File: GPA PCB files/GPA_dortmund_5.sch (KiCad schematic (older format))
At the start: 29 parts, among them U103 AAVID_TO220_HEATSINK, U23 OPA549_KV_11TO-220_11, U24 OPA549_KV_11TO-220_11, U25 INA149SOIC8, X9 MINI-FIT-JR-045569-NA2

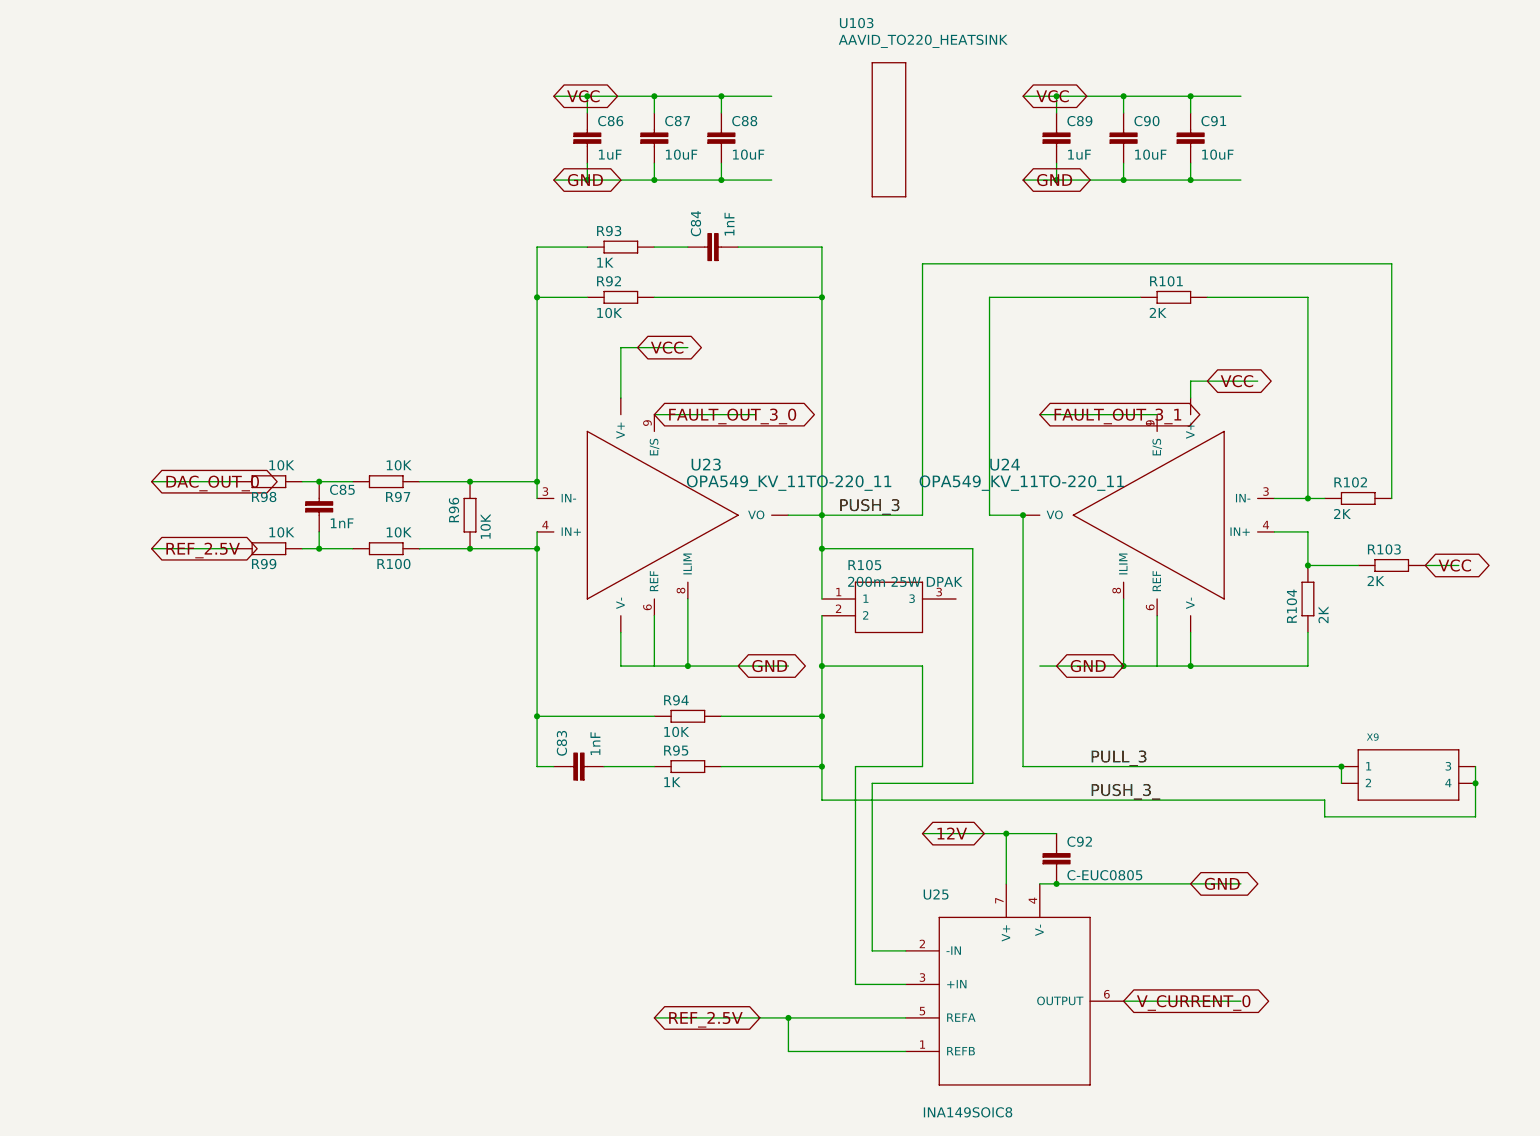
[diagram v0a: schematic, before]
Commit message: fixed schematic after conversion from eagle
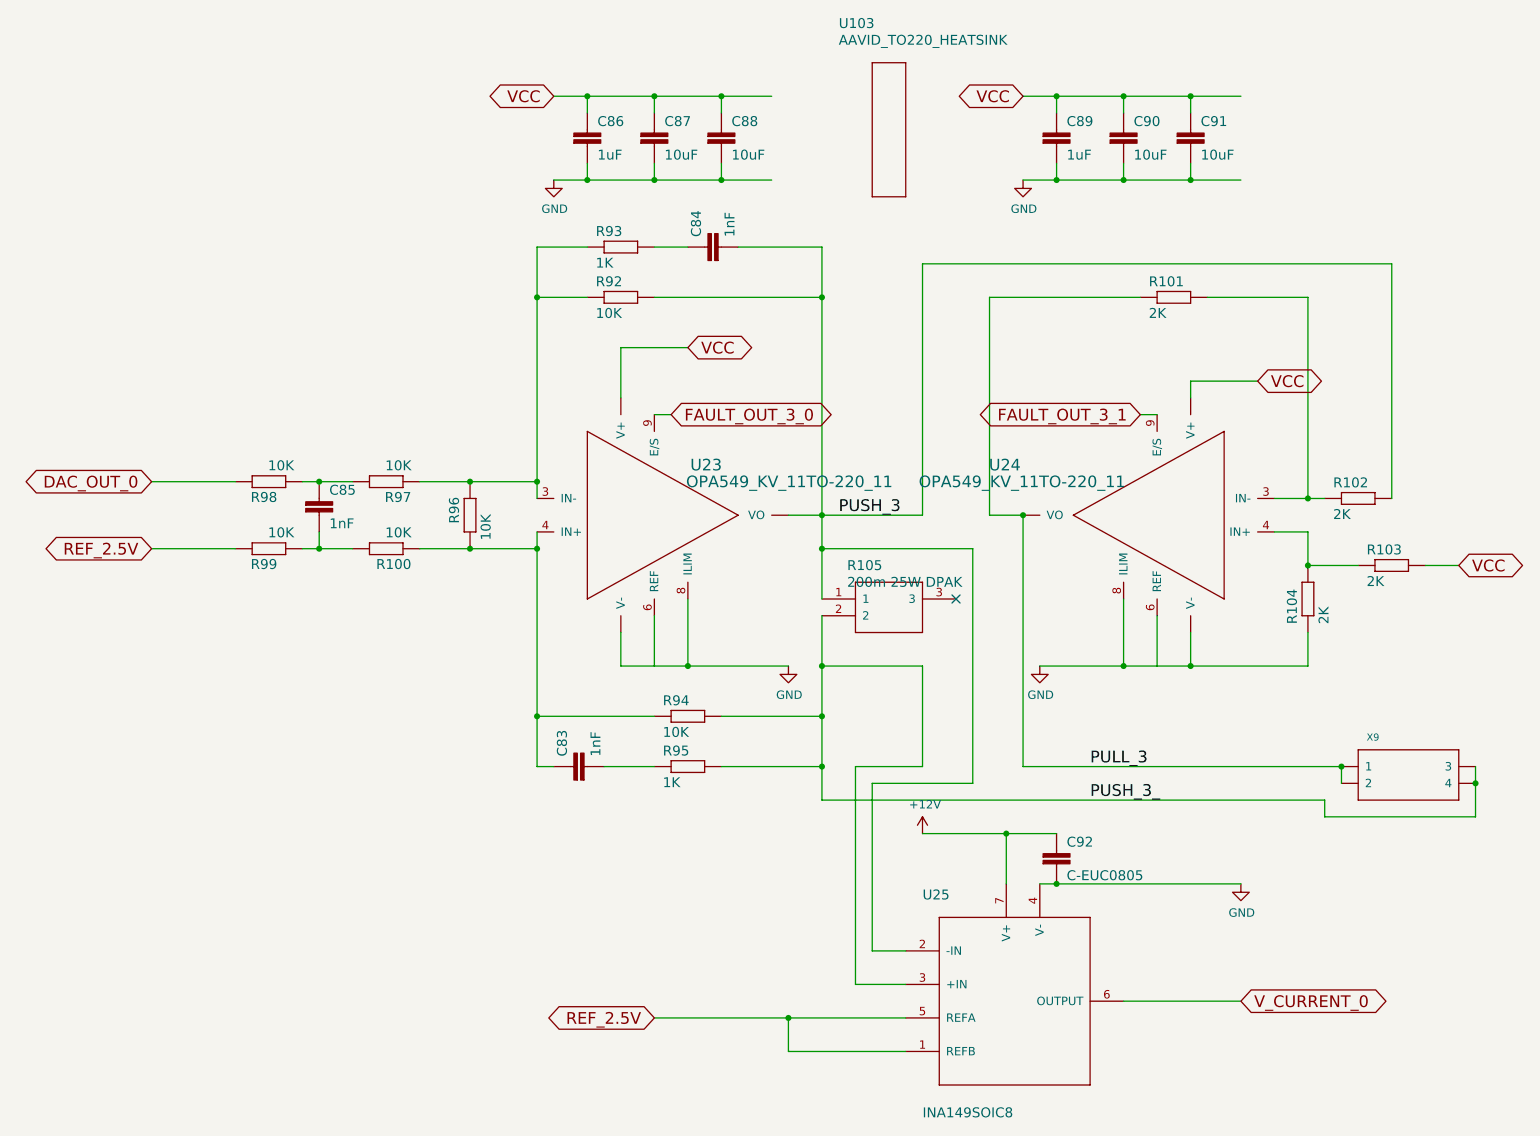
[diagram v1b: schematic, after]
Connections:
- net labels added: +12V
- net labels removed: 12V
- no-connect marks 0 -> 1
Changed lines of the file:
@@
 $Descr A4 11693 8268
 encoding utf-8
-Sheet 1 6
+Sheet 6 6
 Title ""
 Date ""
@@
 Wire Wire Line
 	4600 2800 5000 2800
-Text GLabel 4700 2800 2    70   BiDi ~ 0
+Text GLabel 5000 2800 2    70   BiDi ~ 0
 VCC
 Wire Wire Line
@@
 Wire Wire Line
 	8000 3000 8400 3000
-Text GLabel 8100 3000 2    70   BiDi ~ 0
+Text GLabel 8400 3000 2    70   BiDi ~ 0
 VCC
 Wire Wire Line
 	9400 4100 9600 4100
-Text GLabel 9400 4100 2    70   BiDi ~ 0
+Text GLabel 9600 4100 2    70   BiDi ~ 0
 VCC
 Wire Wire Line
@@
 Connection ~ 4800 1300
 Connection ~ 5200 1300
-Text GLabel 4200 1300 2    70   BiDi ~ 0
+Text GLabel 4200 1300 0    70   BiDi ~ 0
 VCC
 Wire Wire Line
@@
 Connection ~ 7600 1300
 Connection ~ 8000 1300
-Text GLabel 7000 1300 2    70   BiDi ~ 0
+Text GLabel 7000 1300 0    70   BiDi ~ 0
 VCC
 Wire Wire Line
@@
 	5000 4300 5000 4700
 Connection ~ 5000 4700
-Text GLabel 5300 4700 2    70   BiDi ~ 0
-GND
 Wire Wire Line
 	8000 4500 8000 4700
@@
 	8700 4700 8000 4700
 Connection ~ 7600 4700
-Text GLabel 7200 4700 2    70   BiDi ~ 0
-GND
 Connection ~ 8000 4700
 Wire Wire Line
@@
 Connection ~ 4800 1800
 Connection ~ 4400 1800
-Text GLabel 4200 1800 2    70   BiDi ~ 0
-GND
 Wire Wire Line
 	7000 1800 7200 1800
@@
 Connection ~ 7600 1800
 Connection ~ 7200 1800
-Text GLabel 7000 1800 2    70   BiDi ~ 0
-GND
 Wire Wire Line
 	7100 6000 7200 6000
 Wire Wire Line
 	7200 6000 8300 6000
-Text GLabel 8000 6000 2    70   BiDi ~ 0
-GND
 Connection ~ 7200 6000
 Wire Wire Line
@@
 Wire Wire Line
 	2300 4000 1800 4000
-Text GLabel 1800 4000 2    70   BiDi ~ 0
+Text GLabel 1800 4000 0    70   BiDi ~ 0
 REF_2.5V
 Wire Wire Line
@@
 	5600 6800 4800 6800
 Connection ~ 5600 6800
-Text GLabel 4800 6800 2    70   BiDi ~ 0
+Text GLabel 4800 6800 0    70   BiDi ~ 0
 REF_2.5V
 Wire Wire Line
@@
 Wire Wire Line
 	7200 5700 6900 5700
-Text GLabel 6400 5700 2    70   BiDi ~ 0
-12V
 Connection ~ 6900 5700
 Wire Wire Line
-	7800 3200 7100 3200
-Text GLabel 7100 3200 2    70   BiDi ~ 0
+	7800 3200 7700 3200
+Text GLabel 7700 3200 0    70   BiDi ~ 0
 FAULT_OUT_3_1
 Wire Wire Line
-	4800 3200 5400 3200
-Text GLabel 4800 3200 2    70   BiDi ~ 0
+	4800 3200 4900 3200
+Text GLabel 4900 3200 2    70   BiDi ~ 0
 FAULT_OUT_3_0
 Wire Wire Line
 	2300 3600 1800 3600
-Text GLabel 1800 3600 2    70   BiDi ~ 0
+Text GLabel 1800 3600 0    70   BiDi ~ 0
 DAC_OUT_0
 Wire Wire Line
 	7600 6700 8300 6700
-Text GLabel 7600 6700 2    70   BiDi ~ 0
+Text GLabel 8300 6700 2    70   BiDi ~ 0
 V_CURRENT_0
 $Comp
@@
 	1    0    0    -1
 $EndComp
+$Comp
+L power:GND #PWR0128
+U 1 1 61D3A0FD
+P 5600 4700
+F 0 "#PWR0128" H 5600 4450 50  0001 C CNN
+F 1 "GND" H 5605 4527 50  0000 C CNN
+F 2 "" H 5600 4700 50  0001 C CNN
+F 3 "" H 5600 4700 50  0001 C CNN
+	1    5600 4700
+	1    0    0    -1
+$EndComp
+$Comp
+L power:GND #PWR0129
+U 1 1 61D3AA69
+P 7100 4700
+F 0 "#PWR0129" H 7100 4450 50  0001 C CNN
+F 1 "GND" H 7105 4527 50  0000 C CNN
+F 2 "" H 7100 4700 50  0001 C CNN
+F 3 "" H 7100 4700 50  0001 C CNN
+	1    7100 4700
+	1    0    0    -1
+$EndComp
+$Comp
+L power:GND #PWR0130
+U 1 1 61D44618
+P 8300 6000
+F 0 "#PWR0130" H 8300 5750 50  0001 C CNN
+F 1 "GND" H 8305 5827 50  0000 C CNN
+F 2 "" H 8300 6000 50  0001 C CNN
+F 3 "" H 8300 6000 50  0001 C CNN
+	1    8300 6000
+	1    0    0    -1
+$EndComp
+$Comp
+L power:GND #PWR0131
+U 1 1 61D4DEFA
+P 7000 1800
+F 0 "#PWR0131" H 7000 1550 50  0001 C CNN
+F 1 "GND" H 7005 1627 50  0000 C CNN
+F 2 "" H 7000 1800 50  0001 C CNN
+F 3 "" H 7000 1800 50  0001 C CNN
+	1    7000 1800
+	1    0    0    -1
+$EndComp
+$Comp
+L power:GND #PWR0132
+U 1 1 61D578AF
+P 4200 1800
+F 0 "#PWR0132" H 4200 1550 50  0001 C CNN
+F 1 "GND" H 4205 1627 50  0000 C CNN
+F 2 "" H 4200 1800 50  0001 C CNN
+F 3 "" H 4200 1800 50  0001 C CNN
+	1    4200 1800
+	1    0    0    -1
+$EndComp
+$Comp
+L power:+12V #PWR0133
+U 1 1 61D6ACEC
+P 6400 5700
+F 0 "#PWR0133" H 6400 5550 50  0001 C CNN
+F 1 "+12V" H 6415 5873 50  0000 C CNN
+F 2 "" H 6400 5700 50  0001 C CNN
+F 3 "" H 6400 5700 50  0001 C CNN
+	1    6400 5700
+	1    0    0    -1
+$EndComp
+NoConn ~ 6600 4300
 $EndSCHEMATC

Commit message: more schematic fixes, only 1 ERC warning left (but thats ok)
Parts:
- U23, U24: symbol GPA_dortmund-eagle-import:OPA549_KV_11TO-220_11 -> GPA_dortmund-rescue:OPA549_KV_11TO-220_11-GPA_dortmund-eagle-import
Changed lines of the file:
@@
 V_CURRENT_0
 $Comp
-L GPA_dortmund-eagle-import:OPA549_KV_11TO-220_11 U23
+L GPA_dortmund-rescue:OPA549_KV_11TO-220_11-GPA_dortmund-eagle-import U23
 U 1 1 63F53A2D
 P 4700 3800
@@
 $EndComp
 $Comp
-L GPA_dortmund-eagle-import:OPA549_KV_11TO-220_11 U24
+L GPA_dortmund-rescue:OPA549_KV_11TO-220_11-GPA_dortmund-eagle-import U24
 U 1 1 B0DEE33C
 P 7900 3800
